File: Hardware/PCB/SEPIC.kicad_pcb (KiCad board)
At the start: 2 copper layers, 37.5 x 28.5 mm, 34 parts, among them Q1 AO3401A, Q2 AO4262E, U1 LM3478MA

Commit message: Backup update
And some fixes of minor issues
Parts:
- Q1: value AO3401A -> AO4407A; footprint Package_TO_SOT_SMD:SOT-23 -> Package_SO:SOIC-8_3.9x4.9mm_P1.27mm
- R7: value 20m -> 10m
- moved Q1 5.09 mm to (104.8, 57.5)
- moved G*** 1.94 mm to (110.5, 65.2)
- turned Q2 to 180 degrees
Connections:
- C5 pad 2: Net-(Q2-S_1) -> Net-(Q2-D_1)
- L2 pad 2: Net-(Q2-S_1) -> Net-(Q2-D_1)
- Q1 pad 1: Net-(Q1-G) -> Vin
- Q1 pad 3: /Vbus -> Vin
- Q2 pad 1: Net-(Q2-S_1) -> /Isen
- Q2 pad 2: Net-(Q2-S_1) -> /Isen
- Q2 pad 3: Net-(Q2-S_1) -> /Isen
- Q2 pad 5: /Isen -> Net-(Q2-D_1)
- Q2 pad 6: /Isen -> Net-(Q2-D_1)
- Q2 pad 7: /Isen -> Net-(Q2-D_1)
- Q2 pad 8: /Isen -> Net-(Q2-D_1)
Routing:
- net Vin: track 3.72 -> 9.89 mm
- net /Vbus: track 18.5 -> 23.1 mm
- net Net-(Q1-G): track 6.93 -> 10.6 mm
- net /DR: track 24.2 -> 22.5 mm
- net Net-(Q2-S_1): track 0.60 -> 0.00 mm
- net Net-(Q2-D_1): track 0.00 -> 0.60 mm
- added copper zone on F.Cu, net Net-(Q2-D_1)
- removed copper zone on F.Cu, net Net-(Q2-S_1)

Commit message: Update SEPIC PCB: silkscreen, vias, zones
Add title block (title/date/rev/company) and hide bottom testpoint refs. Tweak silkscreen text positions/size and add +/- markings. Rotate/fix SOIC‑8 Q1 footprint orientation and update footprint properties. Swap pad net assignments (Vin ↔ /Vbus) where needed. Add and relocate numerous GND and /Vbus vias, adjust segments, polygons and filled copper shapes, and introduce a /Vbus copper zone to improve connectivity. General PCB layout cleanup to match schematic and improve power/GND routing.
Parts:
- turned Q1 to 180 degrees
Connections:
- Q1 pad 1: Vin -> /Vbus
- Q1 pad 2: Vin -> /Vbus
- Q1 pad 3: Vin -> /Vbus
- Q1 pad 5: /Vbus -> Vin
- Q1 pad 6: /Vbus -> Vin
- Q1 pad 7: /Vbus -> Vin
- Q1 pad 8: /Vbus -> Vin
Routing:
- net Net-(Q1-G): track 10.6 -> 26.6 mm
- net /Vbus: track 23.1 -> 9.12 mm, vias 3 -> 20
- net Vin: track 9.89 -> 11.2 mm
- net GND: vias 51 -> 66
- added copper zone on B.Cu, net /Vbus
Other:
- board text added: "- | +"
- board text added: "Vin : 3-12 V Vout : 3-20 V"
- board text removed: "Vin : 3-12 V Vout : 3-20 V Max power: 30 W"

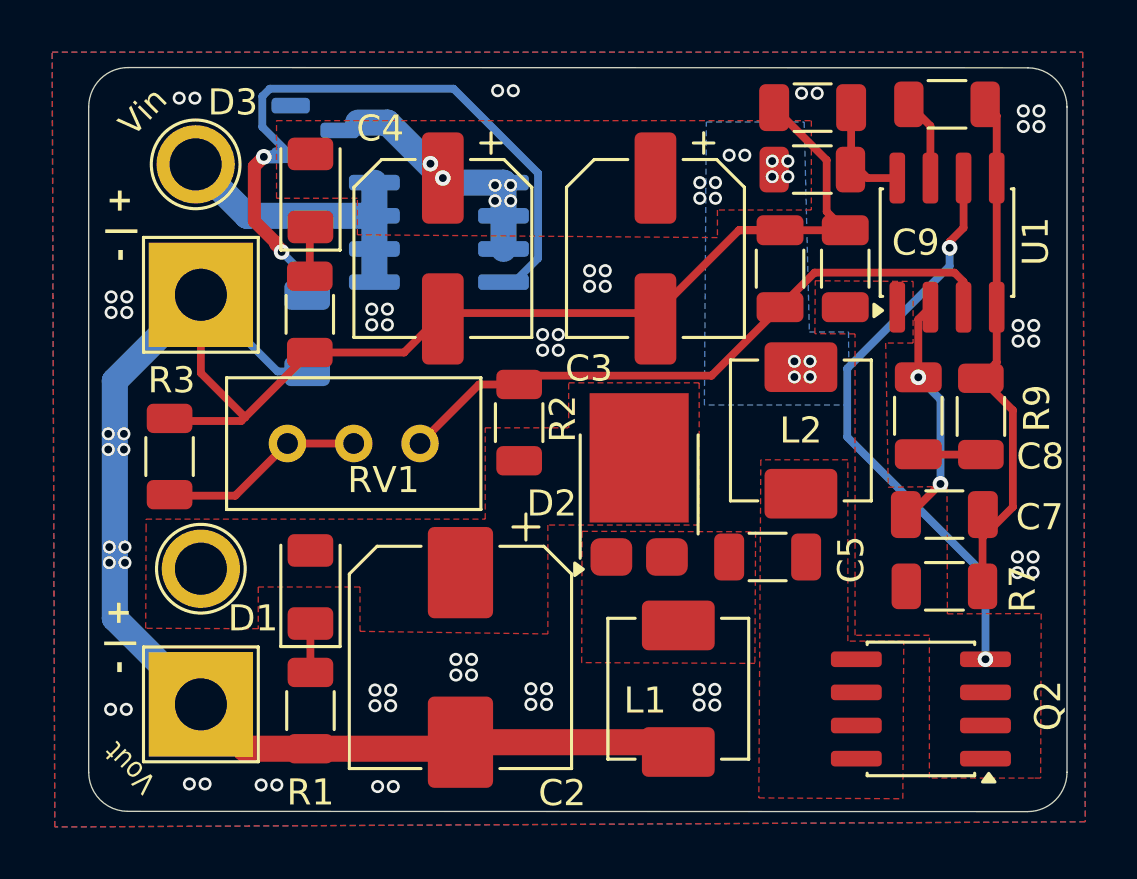
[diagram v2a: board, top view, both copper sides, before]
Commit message: Placed actual coils footprints
Used this:
https://www.tme.eu/pl/details/hcm0703-4r7-r/dlawiki/eaton-electronics/
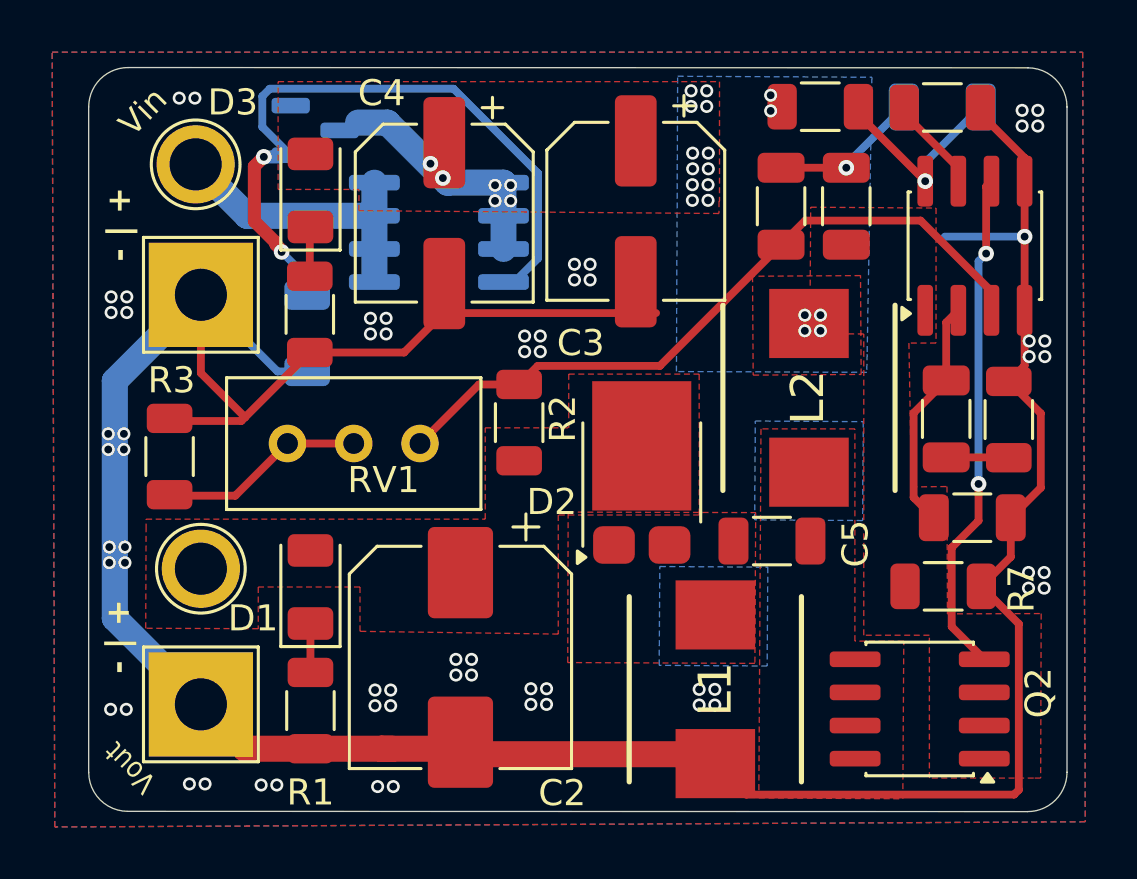
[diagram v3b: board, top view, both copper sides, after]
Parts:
- C6: moved to B.Cu
- L1, L2: value 10u -> 4.7u; footprint Inductor_SMD:L_Vishay_IHLP-2020 -> HCM0703-4R7-R:INDPM7166X300N
- moved C6 4.97 mm to (124.1, 52.7)
- moved R5 2.43 mm to (119.4, 52.7)
- moved C1 2.40 mm to (117.9, 56.5)
- moved C9 2.40 mm to (120.4, 56.5)
- moved C3 1.61 mm to (112.4, 56.7)
- moved L1 1.42 mm to (115.4, 75.0)
- moved C4 1.36 mm to (105.0, 56.8)
- moved L2 1.29 mm to (119.0, 63.9)
- moved R9 1.08 mm to (126.7, 64.7)
- moved U1 1.08 mm to (125.4, 58.0)
- moved C8 1.08 mm to (124.3, 64.7)
- moved C7 1.08 mm to (125.3, 68.4)
- moved C5 0.63 mm to (117.6, 69.3)
- moved D2 0.47 mm to (112.6, 66.7)
- moved R8 0.21 mm to (124.1, 52.7)
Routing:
- net GND: track 105.2 -> 121.2 mm, vias 66 -> 64
- net Net-(U1-V_{IN}): track 4.56 -> 8.24 mm, vias 0 -> 1
- net /DR: track 22.5 -> 19.5 mm
- net /Feedback: track 24.7 -> 27.3 mm
- net Net-(Q2-D_1): track 0.60 -> 0.00 mm
- net Net-(U1-FA/SD): track 3.17 -> 3.68 mm
- net /Isen: track 0.00 -> 0.51 mm
- net Net-(U1-COMP): track 9.13 -> 8.98 mm, vias 2 -> 0
- net /Vbus: track 9.12 -> 9.07 mm, vias 20 -> 24
- added copper zone on B.Cu, net (none)
- added copper zone on F.Cu, net (none)
